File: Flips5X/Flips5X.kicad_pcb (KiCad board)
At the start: 2 copper layers, 100 x 100 mm, 22 parts, among them CN1 Conn_02x30_Odd_Even, CN2 UFP2810, CN3 UFP2810, U1 FP2800A, U2 FP2800A, U3 FP2800A

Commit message: rename L.* and R.* to Y1.* and Y2.*
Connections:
- net /L.A0 renamed /Y1.A0
- net /L.A1 renamed /Y1.A1
- net /L.A2 renamed /Y1.A2
- net /L.B0 renamed /Y1.B0
- net /L.B1 renamed /Y1.B1
- net /L.EN renamed /Y1.EN
- net /L.GND renamed /Y1.GND
- net /L.HV renamed /Y1.HV
- net /L.POL renamed /Y1.POL
- net /L.VCC renamed /Y1.VCC
- net /R.A0 renamed /Y2.A0
- net /R.A1 renamed /Y2.A1
- net /R.A2 renamed /Y2.A2
- net /R.B0 renamed /Y2.B0
- net /R.B1 renamed /Y2.B1
- net /R.EN renamed /Y2.EN
- net /R.GND renamed /Y2.GND
- net /R.HV renamed /Y2.HV
- net /R.POL renamed /Y2.POL
- net /R.VCC renamed /Y2.VCC

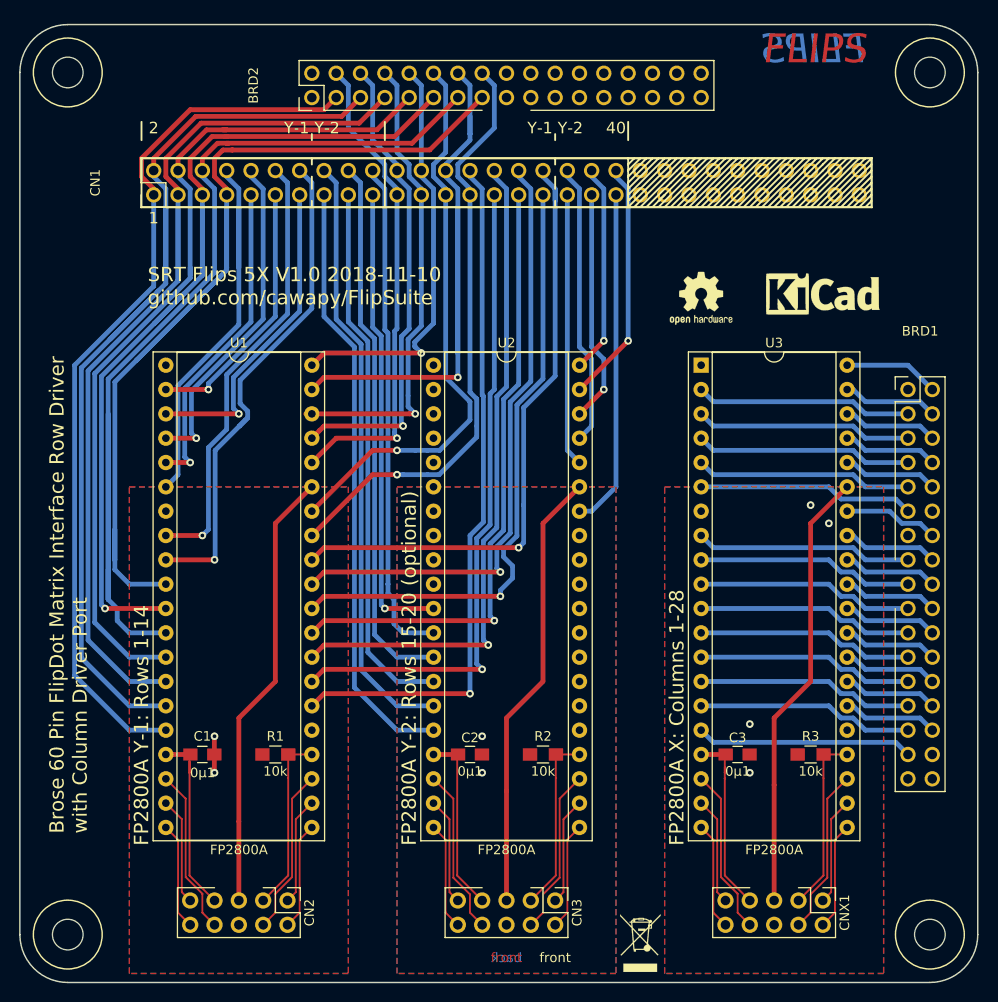
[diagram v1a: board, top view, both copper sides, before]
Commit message: renaming connectors
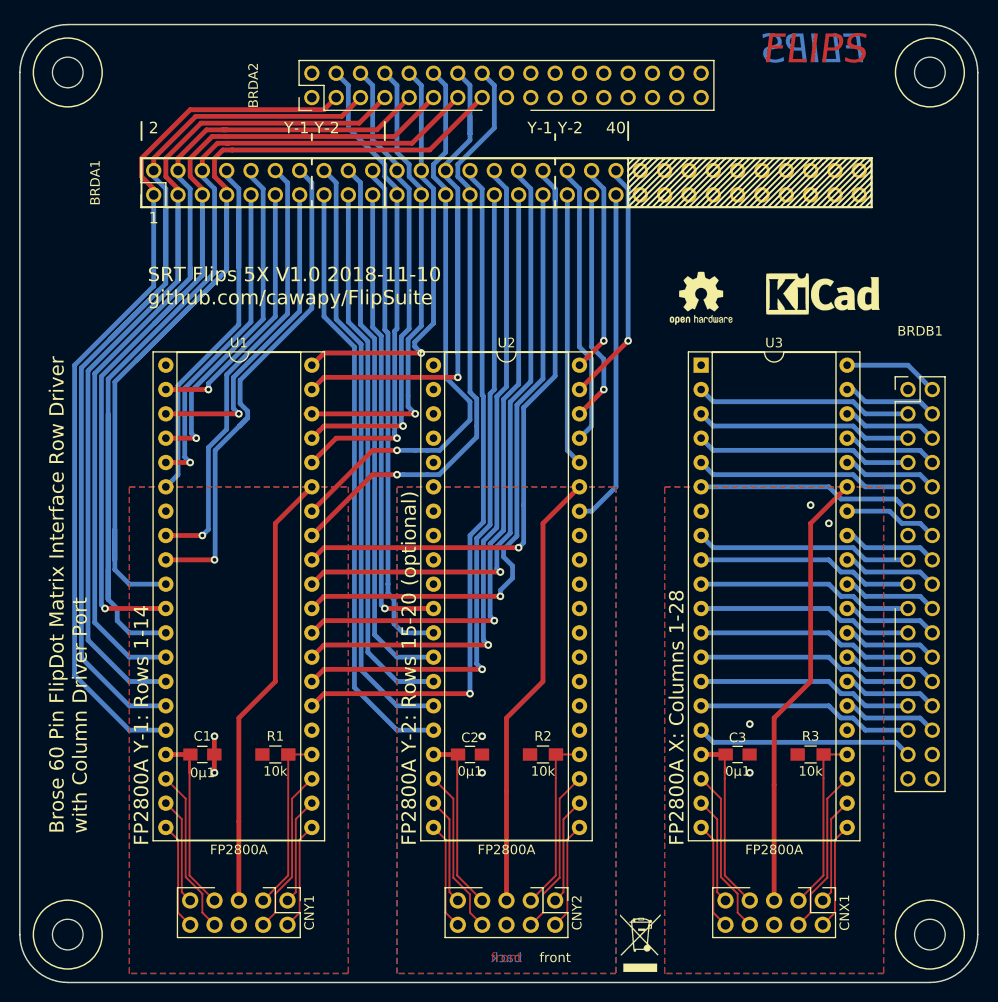
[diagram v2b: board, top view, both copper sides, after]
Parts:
- renumbered CN1 to BRDA1, BRD2 to BRDA2, BRD1 to BRDB1, CN2 to CNY1, CN3 to CNY2

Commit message: fixing DIP connector assignment; adding vias
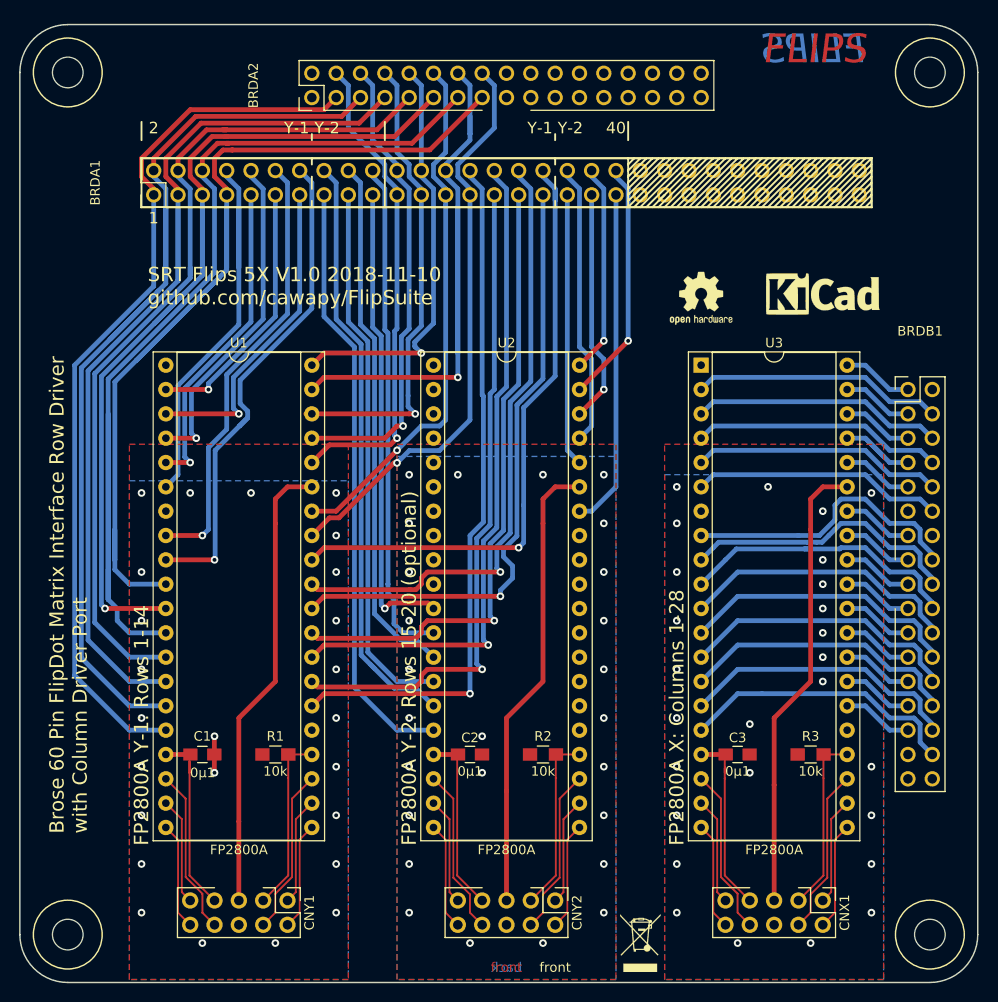
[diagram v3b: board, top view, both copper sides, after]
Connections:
- BRDB1 pad 1: Net-(BRDB1-Pad1) -> /X18
- BRDB1 pad 10: /X15 -> /X9
- BRDB1 pad 11: /X8 -> Net-(BRDB1-Pad11)
- BRDB1 pad 12: Net-(BRDB1-Pad12) -> /X8
- BRDB1 pad 13: Net-(BRDB1-Pad13) -> /X19
- BRDB1 pad 14: /X19 -> Net-(BRDB1-Pad14)
- BRDB1 pad 15: /X12 -> /X21
- BRDB1 pad 16: /X21 -> /X12
- BRDB1 pad 17: /X14 -> /X28
- BRDB1 pad 18: /X28 -> /X14
- BRDB1 pad 19: /X7 -> /X26
- BRDB1 pad 2: /X18 -> Net-(BRDB1-Pad2)
- BRDB1 pad 20: /X26 -> /X7
- BRDB1 pad 21: /X5 -> /X27
- BRDB1 pad 22: /X27 -> /X5
- BRDB1 pad 23: /X6 -> /X25
- BRDB1 pad 24: /X25 -> /X6
- BRDB1 pad 25: /X4 -> /X24
- BRDB1 pad 26: /X24 -> /X4
- BRDB1 pad 27: /X3 -> /X23
- BRDB1 pad 28: /X23 -> /X3
- BRDB1 pad 29: /X2 -> /X22
- BRDB1 pad 3: /X11 -> /X20
- BRDB1 pad 30: /X22 -> /X2
- BRDB1 pad 31: /X1 -> Net-(BRDB1-Pad31)
- BRDB1 pad 32: Net-(BRDB1-Pad32) -> /X1
- BRDB1 pad 4: /X20 -> /X11
- BRDB1 pad 5: /X13 -> /X17
- BRDB1 pad 6: /X17 -> /X13
- BRDB1 pad 7: /X10 -> /X16
- BRDB1 pad 8: /X16 -> /X10
- BRDB1 pad 9: /X9 -> /X15
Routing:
- net /X12: track 22.6 -> 30.4 mm
- net /X7: track 22.6 -> 30.0 mm
- net /X14: track 22.6 -> 29.5 mm
- net /X6: track 22.6 -> 29.5 mm
- net /X3: track 22.6 -> 29.5 mm
- net /X5: track 22.6 -> 29.5 mm
- net /X4: track 22.6 -> 29.5 mm
- net /X2: track 22.6 -> 29.5 mm
- net /X1: track 22.6 -> 29.5 mm
- net /X11: track 22.6 -> 26.2 mm
- net /X10: track 22.6 -> 26.2 mm
- net /X9: track 22.6 -> 26.2 mm
- net /X13: track 22.6 -> 26.2 mm
- net /X8: track 22.6 -> 26.2 mm
- net /RY5: track 59.3 -> 55.7 mm
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
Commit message: Fixing 34 Pin interface pin mapping; renaming RYnn to ~RYnn
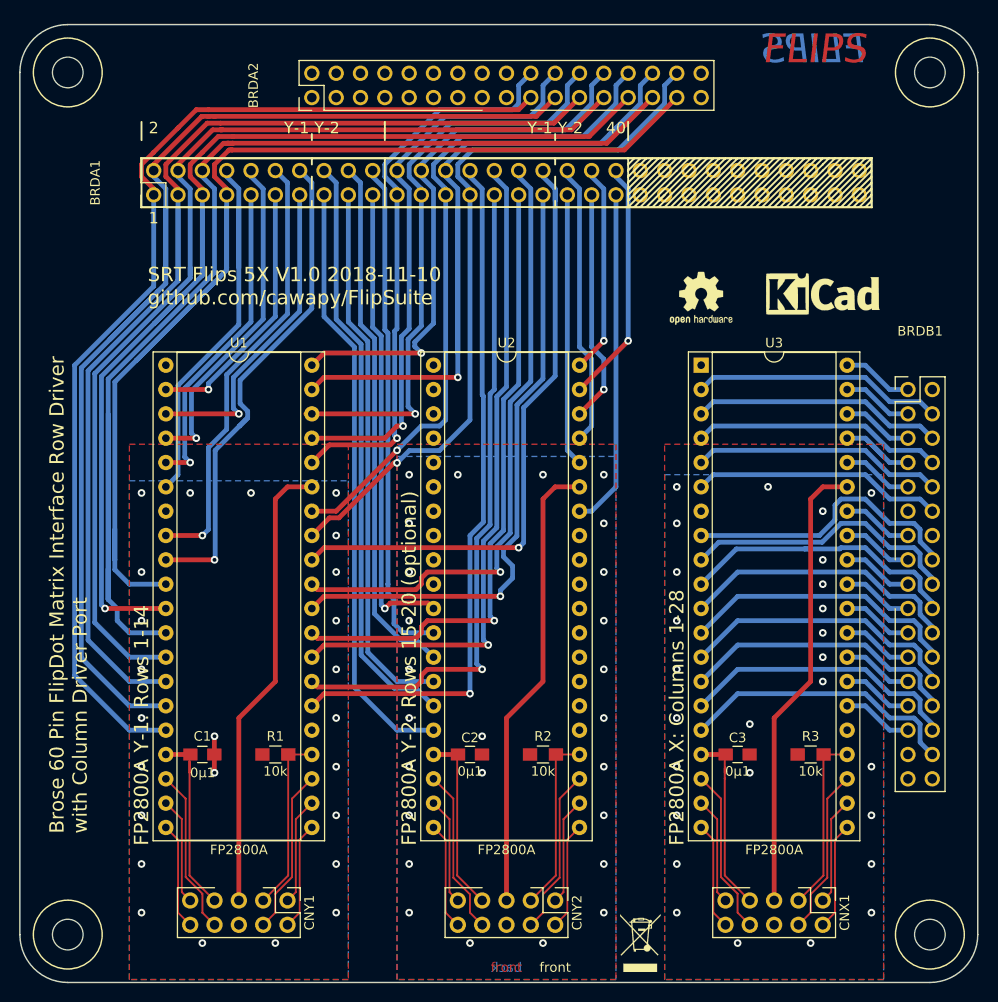
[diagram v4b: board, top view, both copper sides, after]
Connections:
- net /RY10 renamed /~RY10
- net /RY11 renamed /~RY11
- net /RY12 renamed /~RY12
- net /RY13 renamed /~RY13
- net /RY14 renamed /~RY14
- net /RY15 renamed /~RY15
- net /RY16 renamed /~RY16
- net /RY17 renamed /~RY17
- net /RY18 renamed /~RY18
- net /RY19 renamed /~RY19
- net /RY20 renamed /~RY20
- net /RY8 renamed /~RY8
- net /RY9 renamed /~RY9
- BRDA1 pad 21: /RY1 -> /~RY1
- BRDA1 pad 22: /RY2 -> /~RY2
- BRDA1 pad 23: /RY3 -> /~RY3
- BRDA1 pad 24: /RY4 -> /~RY4
- BRDA1 pad 25: /RY5 -> /~RY5
- BRDA1 pad 26: /RY6 -> /~RY6
- BRDA1 pad 27: /RY7 -> /~RY7
- BRDA2 pad 10: /RY4 -> Net-(BRDA2-Pad10)
- BRDA2 pad 11: /SY5 -> Net-(BRDA2-Pad11)
- BRDA2 pad 12: /RY5 -> Net-(BRDA2-Pad12)
- BRDA2 pad 13: /SY6 -> Net-(BRDA2-Pad13)
- BRDA2 pad 14: /RY6 -> Net-(BRDA2-Pad14)
- BRDA2 pad 15: /SY7 -> Net-(BRDA2-Pad15)
- BRDA2 pad 16: /RY7 -> Net-(BRDA2-Pad16)
- BRDA2 pad 19: Net-(BRDA2-Pad19) -> /SY1
- BRDA2 pad 20: Net-(BRDA2-Pad20) -> /~RY1
- BRDA2 pad 21: Net-(BRDA2-Pad21) -> /SY2
- BRDA2 pad 22: Net-(BRDA2-Pad22) -> /~RY2
- BRDA2 pad 23: Net-(BRDA2-Pad23) -> /SY3
- BRDA2 pad 24: Net-(BRDA2-Pad24) -> /~RY3
- BRDA2 pad 25: Net-(BRDA2-Pad25) -> /SY4
- BRDA2 pad 26: Net-(BRDA2-Pad26) -> /~RY4
- BRDA2 pad 27: Net-(BRDA2-Pad27) -> /SY5
- BRDA2 pad 28: Net-(BRDA2-Pad28) -> /~RY5
- BRDA2 pad 29: Net-(BRDA2-Pad29) -> /SY6
- BRDA2 pad 3: /SY1 -> Net-(BRDA2-Pad3)
- BRDA2 pad 30: Net-(BRDA2-Pad30) -> /~RY6
- BRDA2 pad 31: Net-(BRDA2-Pad31) -> /SY7
- BRDA2 pad 32: Net-(BRDA2-Pad32) -> /~RY7
- BRDA2 pad 4: /RY1 -> Net-(BRDA2-Pad4)
- BRDA2 pad 5: /SY2 -> Net-(BRDA2-Pad5)
- BRDA2 pad 6: /RY2 -> Net-(BRDA2-Pad6)
- BRDA2 pad 7: /SY3 -> Net-(BRDA2-Pad7)
- BRDA2 pad 8: /RY3 -> Net-(BRDA2-Pad8)
- BRDA2 pad 9: /SY4 -> Net-(BRDA2-Pad9)
- U1 pad 33: /RY7 -> /~RY7
- U1 pad 34: /RY5 -> /~RY5
- U1 pad 36: /RY1 -> /~RY1
- U1 pad 37: /RY2 -> /~RY2
- U1 pad 38: /RY3 -> /~RY3
- U1 pad 39: /RY6 -> /~RY6
- U1 pad 40: /RY4 -> /~RY4
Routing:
- net /~RY6: track 0.00 -> 81.3 mm, vias 0 -> 1
- net /~RY7: track 0.00 -> 76.0 mm, vias 0 -> 1
- net /~RY5: track 0.00 -> 70.5 mm, vias 0 -> 1
- net /RY6: track 66.8 -> 0.00 mm, vias 1 -> 0
- net /~RY3: track 0.00 -> 61.7 mm, vias 0 -> 1
- net /~RY2: track 0.00 -> 59.9 mm, vias 0 -> 1
- net /RY7: track 59.7 -> 0.00 mm, vias 1 -> 0
- net /~RY1: track 0.00 -> 59.5 mm, vias 0 -> 1
- net /~RY4: track 0.00 -> 57.4 mm, vias 0 -> 1
- net /RY5: track 55.7 -> 0.00 mm, vias 1 -> 0
- net /RY1: track 50.9 -> 0.00 mm, vias 1 -> 0
- net /RY3: track 49.5 -> 0.00 mm, vias 1 -> 0
- net /RY2: track 49.4 -> 0.00 mm, vias 1 -> 0
- net /RY4: track 43.4 -> 0.00 mm, vias 1 -> 0
- net /SY6: track 111.4 -> 132.0 mm
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
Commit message: single GND, VCC, HV for Flips5X
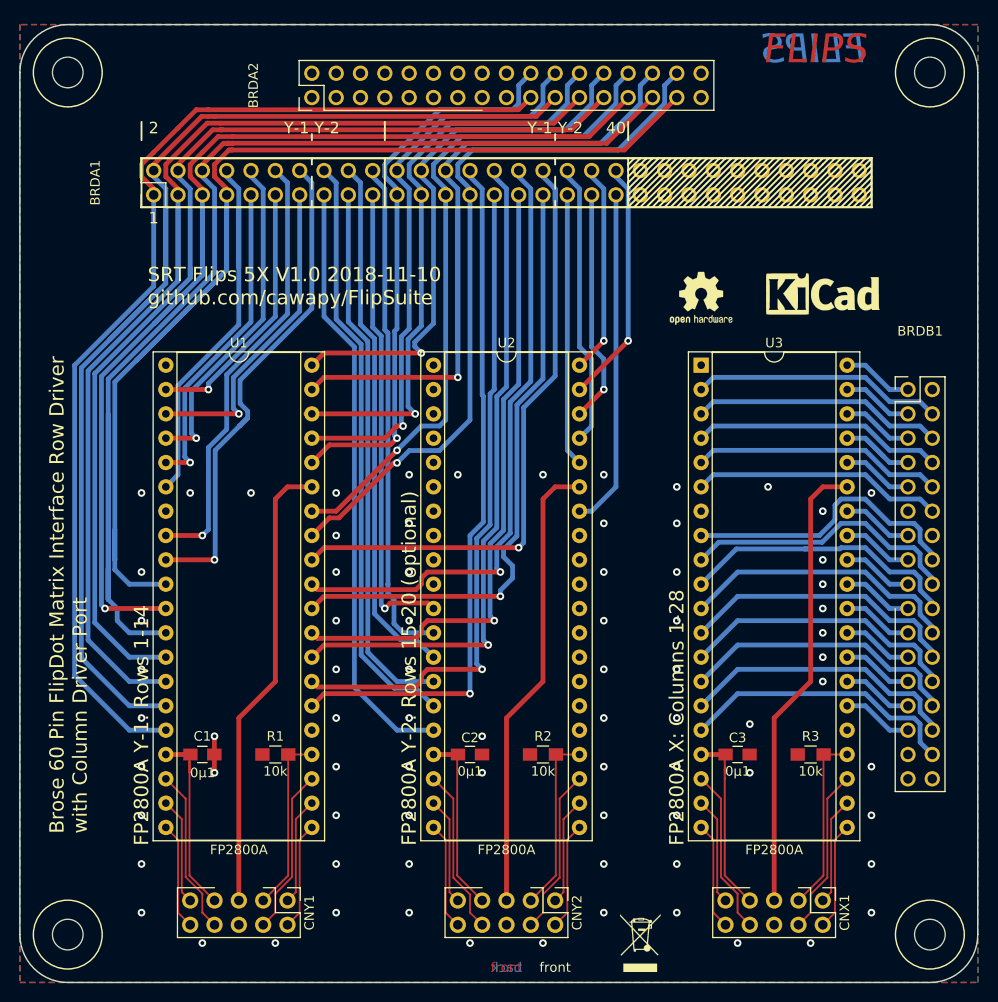
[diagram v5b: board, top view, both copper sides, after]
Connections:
- C1 pad 1: /Y1.GND -> /GND
- C1 pad 2: /Y1.VCC -> /VCC
- C2 pad 1: /Y2.VCC -> /VCC
- C2 pad 2: /Y2.GND -> /GND
- C3 pad 1: /X.VCC -> /VCC
- C3 pad 2: /X.GND -> /GND
- CNX1 pad 5: /X.HV -> /HV
- CNX1 pad 6: /X.GND -> /GND
- CNX1 pad 7: /X.VCC -> /VCC
- CNY1 pad 5: /Y1.HV -> /HV
- CNY1 pad 6: /Y1.GND -> /GND
- CNY1 pad 7: /Y1.VCC -> /VCC
- CNY2 pad 5: /Y2.HV -> /HV
- CNY2 pad 6: /Y2.GND -> /GND
- CNY2 pad 7: /Y2.VCC -> /VCC
- R1 pad 1: /Y1.GND -> /GND
- R2 pad 1: /Y2.GND -> /GND
- R3 pad 1: /X.GND -> /GND
- U1 pad 17: /Y1.VCC -> /VCC
- U1 pad 25: /Y1.GND -> /GND
- U1 pad 35: /Y1.HV -> /HV
- U1 pad 7: /Y1.GND -> /GND
- U2 pad 17: /Y2.VCC -> /VCC
- U2 pad 25: /Y2.GND -> /GND
- U2 pad 35: /Y2.HV -> /HV
- U2 pad 7: /Y2.GND -> /GND
- U3 pad 17: /X.VCC -> /VCC
- U3 pad 25: /X.GND -> /GND
- U3 pad 35: /X.HV -> /HV
- U3 pad 7: /X.GND -> /GND
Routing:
- net /HV: track 0.00 -> 143.5 mm
- net /VCC: track 0.00 -> 58.6 mm
- net /Y1.HV: track 47.8 -> 0.00 mm
- net /Y2.HV: track 47.8 -> 0.00 mm
- net /X.HV: track 47.8 -> 0.00 mm
- net /Y1.VCC: track 20.1 -> 0.00 mm
- net /X.VCC: track 19.6 -> 0.00 mm
- net /Y2.VCC: track 18.9 -> 0.00 mm
- net /GND: track 0.00 -> 3.91 mm, vias 0 -> 78
- net /Y1.GND: track 3.83 -> 0.00 mm, vias 25 -> 0
- net /Y2.GND: track 0.06 -> 0.00 mm, vias 26 -> 0
- net /X.GND: track 0.03 -> 0.00 mm, vias 27 -> 0
- added copper zone on B.Cu, net /GND
- added copper zone on F.Cu, net /GND
- removed copper zone on B.Cu, net /X.GND
- removed copper zone on F.Cu, net /X.GND
- removed copper zone on B.Cu, net /Y1.GND
- removed copper zone on F.Cu, net /Y1.GND
- removed copper zone on B.Cu, net /Y2.GND
- removed copper zone on F.Cu, net /Y2.GND
